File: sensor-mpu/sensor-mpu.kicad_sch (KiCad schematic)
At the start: 20 parts, among them J4 JST SH 1.0, Q6 BSS138, Q7 BSS138, U11 MAX30102, U12 LN1134A182MR-G, U13 MPU-9250

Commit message: Downgrade and pcb breakdown
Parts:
- removed C24: 1uF 16V, Capacitor_SMD:C_0603_1608Metric, symbol Device:C_Small
- removed C25: 2.2uF 16V, Capacitor_SMD:C_0603_1608Metric, symbol Device:C_Small
- removed C26: 10nF 16V, Capacitor_SMD:C_0603_1608Metric, symbol Device:C_Small
- removed C27, C28: 100nF 16V, Capacitor_SMD:C_0603_1608Metric, symbol Device:C_Small
- removed J4: JST SH 1.0, Connector_JST:JST_SH_SM04B-SRSS-TB_1x04-1MP_P1.00mm_Horizontal, symbol Connector_Generic_MountingPin:Conn_01x04_MountingPin
- removed Q6, Q7: BSS138, Package_TO_SOT_SMD:SOT-23, symbol Transistor_FET:BSS138
- removed R32, R33, R34, R35: 10K, Resistor_SMD:R_0603_1608Metric, symbol Device:R
- removed R36: 0R, Resistor_SMD:R_0402_1005Metric, symbol Device:R
- removed R37: 10K, Resistor_SMD:R_0402_1005Metric, symbol Device:R
- removed TP13, TP15: INT, TestPoint:TestPoint_Pad_D1.0mm, symbol Connector:TestPoint
- removed TP14: FSYNC, TestPoint:TestPoint_Pad_D1.0mm, symbol Connector:TestPoint
- removed U11: MAX30102, OptoDevice:Maxim_OLGA-14_3.3x5.6mm_P0.8mm, symbol Sensor:MAX30102
- removed U12: LN1134A182MR-G, Package_TO_SOT_SMD:SOT-23-5, symbol Regulator_Linear:AP2112K-1.8
- removed U13: MPU-9250, Sensor_Motion:InvenSense_QFN-24_3x3mm_P0.4mm_NoMask, symbol Sensor_Motion:MPU-9250
- added C1: 1uF 16V, Capacitor_SMD:C_0603_1608Metric, symbol Device:C_Small
- added C2: 10nF 16V, Capacitor_SMD:C_0603_1608Metric, symbol Device:C_Small
- added C3: 2.2uF 16V, Capacitor_SMD:C_0603_1608Metric, symbol Device:C_Small
- added C4, C5: 100nF 16V, Capacitor_SMD:C_0603_1608Metric, symbol Device:C_Small
- added J1: JST SH1.0, Connector_JST:JST_SH_SM04B-SRSS-TB_1x04-1MP_P1.00mm_Horizontal, symbol Connector_Generic_MountingPin:Conn_01x04_MountingPin
- added Q1, Q2: BSS138, Package_TO_SOT_SMD:SOT-23, symbol Transistor_FET:BSS138
- added R1: 0R, Resistor_SMD:R_0402_1005Metric, symbol Device:R
- added R2, R3, R4, R5, R6: 10K, Resistor_SMD:R_0402_1005Metric, symbol Device:R
- added TP1: MPU_FSYNC, TestPoint:TestPoint_Pad_D1.0mm, symbol Connector:TestPoint
- added TP2: MPU_INT, TestPoint:TestPoint_Pad_D1.0mm, symbol Connector:TestPoint
- added TP3: MAX_INT, TestPoint:TestPoint_Pad_D1.0mm, symbol Connector:TestPoint
- added U1: LN1134A182MR-G, Package_TO_SOT_SMD:SOT-23-5, symbol Regulator_Linear:AP2112K-3.3
- added U2: MPU-9250, Sensor_Motion:InvenSense_QFN-24_3x3mm_P0.4mm, symbol Sensor_Motion:MPU-9250
- added U3: MAX30102, OptoDevice:Maxim_OLGA-14_3.3x5.6mm_P0.8mm, symbol Sensor:MAX30102
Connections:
- net +1V8: now also Q1.1 (G), Q2.1 (G), R3.1, R4.1, U3.11 (VDD)
- net +3V3: now also C1.1, C2.1, C3.1, C4.1, J1.3 (Pin_3), R1.1, R5.2, R6.2, U1.1 (VIN), U1.3 (EN), U1.5 (VOUT), U2.1 (RESV_VDDIO), U2.13 (VDD), U2.22 (~{CS}), U2.8 (VDDIO), U3.10 (VLED+), U3.9 (VLED+)
- net GND: now also C1.2, C2.2, C3.2, C4.2, C5.2, J1.4 (Pin_4), R2.2, U1.2 (GND), U2.18 (GND), U2.20 (RESV_GND), U3.12 (GND), U3.4 (PGND)
- net SCL: now also J1.2 (Pin_2), Q1.3 (D), R6.1, U2.23 (SCL/SCLK)
- net SCL_1V8: now also Q1.2 (S), R4.2, U3.2 (SCL)
- net SDA: now also J1.1 (Pin_1), Q2.3 (D), R5.1, U2.24 (SDA/MOSI)
- net SDA_1V8: now also Q2.2 (S), R3.2, U3.3 (SDA)
- new net: R1.2, R2.1, U2.9 (AD0/MISO)
- new net: TP3.1, U3.13 (~{INT})
- new net: C5.1, U2.10 (REGOUT)
- new net: TP1.1, U2.11 (FSYNC)
- new net: TP2.1, U2.12 (INT)
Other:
- note added: "JST Port"
- title: (none) -> sensor-unit-mpu

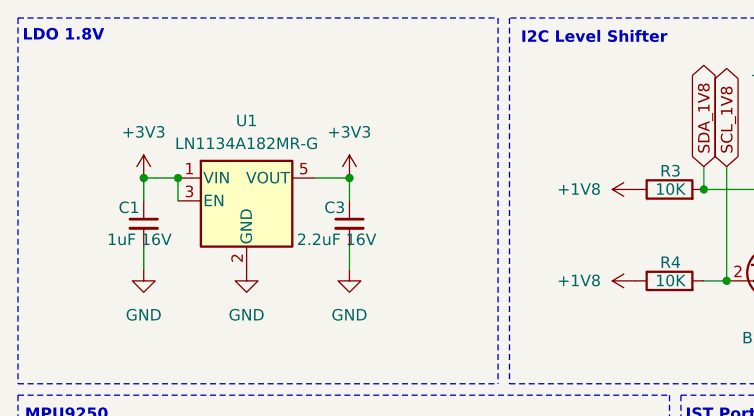
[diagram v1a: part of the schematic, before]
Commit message: add sensor board
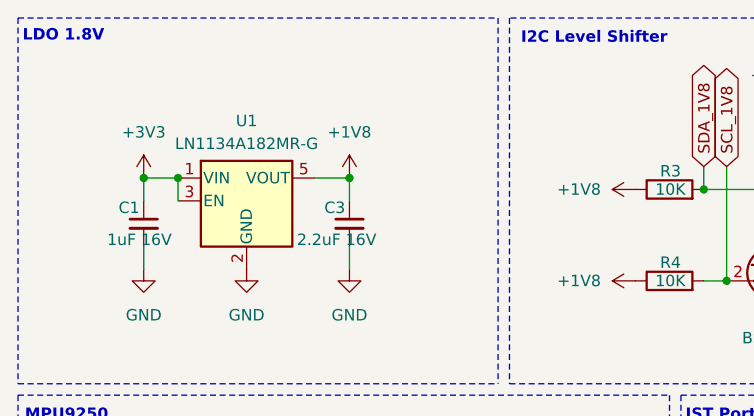
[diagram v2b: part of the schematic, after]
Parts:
- U2: footprint Sensor_Motion:InvenSense_QFN-24_3x3mm_P0.4mm -> Sensor_Motion:InvenSense_QFN-24_3x3mm_P0.4mm_NoMask
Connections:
- net +1V8: now also C3.1, U1.5 (VOUT)
- net +3V3: no longer C3.1, U1.5 (VOUT)
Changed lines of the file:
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@@
 	)
 	(junction
-		(at 49.53 30.48)
+		(at 67.31 76.2)
 		(diameter 0)
 		(color 0 0 0 0)
 	)
 	(junction
-		(at 67.31 76.2)
+		(at 109.22 41.91)
 		(diameter 0)
 		(color 0 0 0 0)
 	)
 	(junction
-		(at 109.22 41.91)
+		(at 30.48 30.48)
 		(diameter 0)
 		(color 0 0 0 0)
 	)
 	(junction
-		(at 30.48 30.48)
+		(at 49.53 30.48)
 		(diameter 0)
 		(color 0 0 0 0)
@@
 	)
 	(symbol
-		(lib_id "power:+3V3")
-		(at 49.53 30.48 0)
-		(unit 1)
-		(exclude_from_sim no)
-		(in_bom yes)
-		(on_board yes)
-		(dnp no)
-		(fields_autoplaced yes)
-		(property "Reference" "#PWR09"
-			(at 49.53 34.29 0)
-			(effects
-				(font
-					(size 1.27 1.27)
-				)
-				(hide yes)
-			)
-		)
-		(property "Value" "+3V3"
-			(at 49.53 25.4 0)
-			(effects
-				(font
-					(size 1.27 1.27)
-				)
-			)
-		)
-		(property "Footprint" ""
-			(at 49.53 30.48 0)
-			(effects
-				(font
-					(size 1.27 1.27)
-				)
-				(hide yes)
-			)
-		)
-		(property "Datasheet" ""
-			(at 49.53 30.48 0)
-			(effects
-				(font
-					(size 1.27 1.27)
-				)
-				(hide yes)
-			)
-		)
-		(property "Description" "Power symbol creates a global label with name \"+3V3\""
-			(at 49.53 30.48 0)
-			(effects
-				(font
-					(size 1.27 1.27)
-				)
-				(hide yes)
-			)
-		)
-		(pin "1"
-		)
-		(instances
-			(project "sensor-mpu"
-				(path "/31073d40-5b6d-4842-a1db-ec3bf1713456"
-					(reference "#PWR09")
-					(unit 1)
-				)
-			)
-		)
-	)
-	(symbol
 		(lib_id "Sensor:MAX30102")
 		(at 158.75 41.91 270)
@@
 			)
 		)
-		(property "Footprint" "Sensor_Motion:InvenSense_QFN-24_3x3mm_P0.4mm"
+		(property "Footprint" "Sensor_Motion:InvenSense_QFN-24_3x3mm_P0.4mm_NoMask"
 			(at 48.26 124.46 0)
 			(effects
@@
 		(pin "8"
 		)
+		(pin "14"
+		)
+		(pin "5"
+		)
+		(pin "6"
+		)
+		(pin "17"
+		)
+		(pin "16"
+		)
+		(pin "15"
+		)
+		(pin "2"
+		)
+		(pin "4"
+		)
+		(pin "3"
+		)
+		(pin "19"
+		)
 		(instances
 			(project ""
@@
 					(unit 1)
 				)
+			)
+		)
+	)
+	(symbol
+		(lib_id "power:+1V8")
+		(at 49.53 30.48 0)
+		(unit 1)
+		(exclude_from_sim no)
+		(in_bom yes)
+		(on_board yes)
+		(dnp no)
+		(fields_autoplaced yes)
+		(property "Reference" "#PWR09"
+			(at 49.53 34.29 0)
+			(effects
+				(font
+					(size 1.27 1.27)
+				)
+				(hide yes)
+			)
+		)
+		(property "Value" "+1V8"
+			(at 49.53 25.4 0)
+			(effects
+				(font
+					(size 1.27 1.27)
+				)
+			)
+		)
+		(property "Footprint" ""
+			(at 49.53 30.48 0)
+			(effects
+				(font
+					(size 1.27 1.27)
+				)
+				(hide yes)
+			)
+		)
+		(property "Datasheet" ""
+			(at 49.53 30.48 0)
+			(effects
+				(font
+					(size 1.27 1.27)
+				)
+				(hide yes)
+			)
+		)
+		(property "Description" "Power symbol creates a global label with name \"+1V8\""
+			(at 49.53 30.48 0)
+			(effects
+				(font
+					(size 1.27 1.27)
+				)
+				(hide yes)
+			)
+		)
+		(pin "1"
+		)
+		(instances
+			(project "sensor-mpu"
+				(path "/31073d40-5b6d-4842-a1db-ec3bf1713456"
+					(reference "#PWR09")
+					(unit 1)
+				)
